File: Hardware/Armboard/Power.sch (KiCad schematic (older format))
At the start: 15 parts

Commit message: H-Bridge completed
Completed the H-Bridge Hierarchal Sheet
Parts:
- J?: symbol MRDT_Connectors:Test_Point -> Armboard-rescue:Test_Point-MRDT_Connectors
- U?: symbol MRDT_Devices:LM2576D2TR4 -> Armboard-rescue:LM2576D2TR4-MRDT_Devices
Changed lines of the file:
@@
 $EndComp
 $Comp
-L MRDT_Devices:LM2576D2TR4 U?
+L Armboard-rescue:LM2576D2TR4-MRDT_Devices U?
 U 1 1 5F74DE4A
 P 2100 3900
@@
 	3800 4250 3800 4200
 $Comp
-L MRDT_Connectors:Test_Point J?
+L Armboard-rescue:Test_Point-MRDT_Connectors J?
 U 1 1 5F75C39D
 P 4550 3950

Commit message: Added serial pins, limit switches, titles, and indicators
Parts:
- removed D?: D_Zener, symbol Device:D_Zener
- added Conn? (x6): AndersonPP, symbol Armboard-rescue:AndersonPP-MRDT_Connectors-Armboard-rescue-Armboard-rescue-Armb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
- added D?: D_Schottky, symbol Device:D_Schottky
- added D? (x2): LED, symbol Device:LED
- added R?: 500, symbol Device:R
- added R?: 330, symbol Device:R
- J?: symbol Armboard-rescue:Test_Point-MRDT_Connectors -> Armboard-rescue:Test_Point-MRDT_Connectors-Armboard-rescue
- U?: symbol Armboard-rescue:LM2576D2TR4-MRDT_Devices -> Armboard-rescue:LM2576D2TR4-MRDT_Devices-Armboard-rescue
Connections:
- net +12V: now also R?.2
- net +12VA: now also Conn?.3 (V+Act), Conn?.3 (V+Act), Conn?.3 (V+Act)
- net +3V3: now also R?.2
- net GND: now also Conn?.1 (GND), Conn?.1 (GND), Conn?.1 (GND), D?.1 (K), D?.1 (K), D?.1 (K)
- net at L?.2, U?.2 (OUTPUT): now also D?.2 (A)
- new net: D?.2 (A), R?.1 (x2)
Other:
- note added: "Output Andersons"
- note added: "Power"
- moved on the sheet: C7, C8, D?, J?, L?, R?, U?

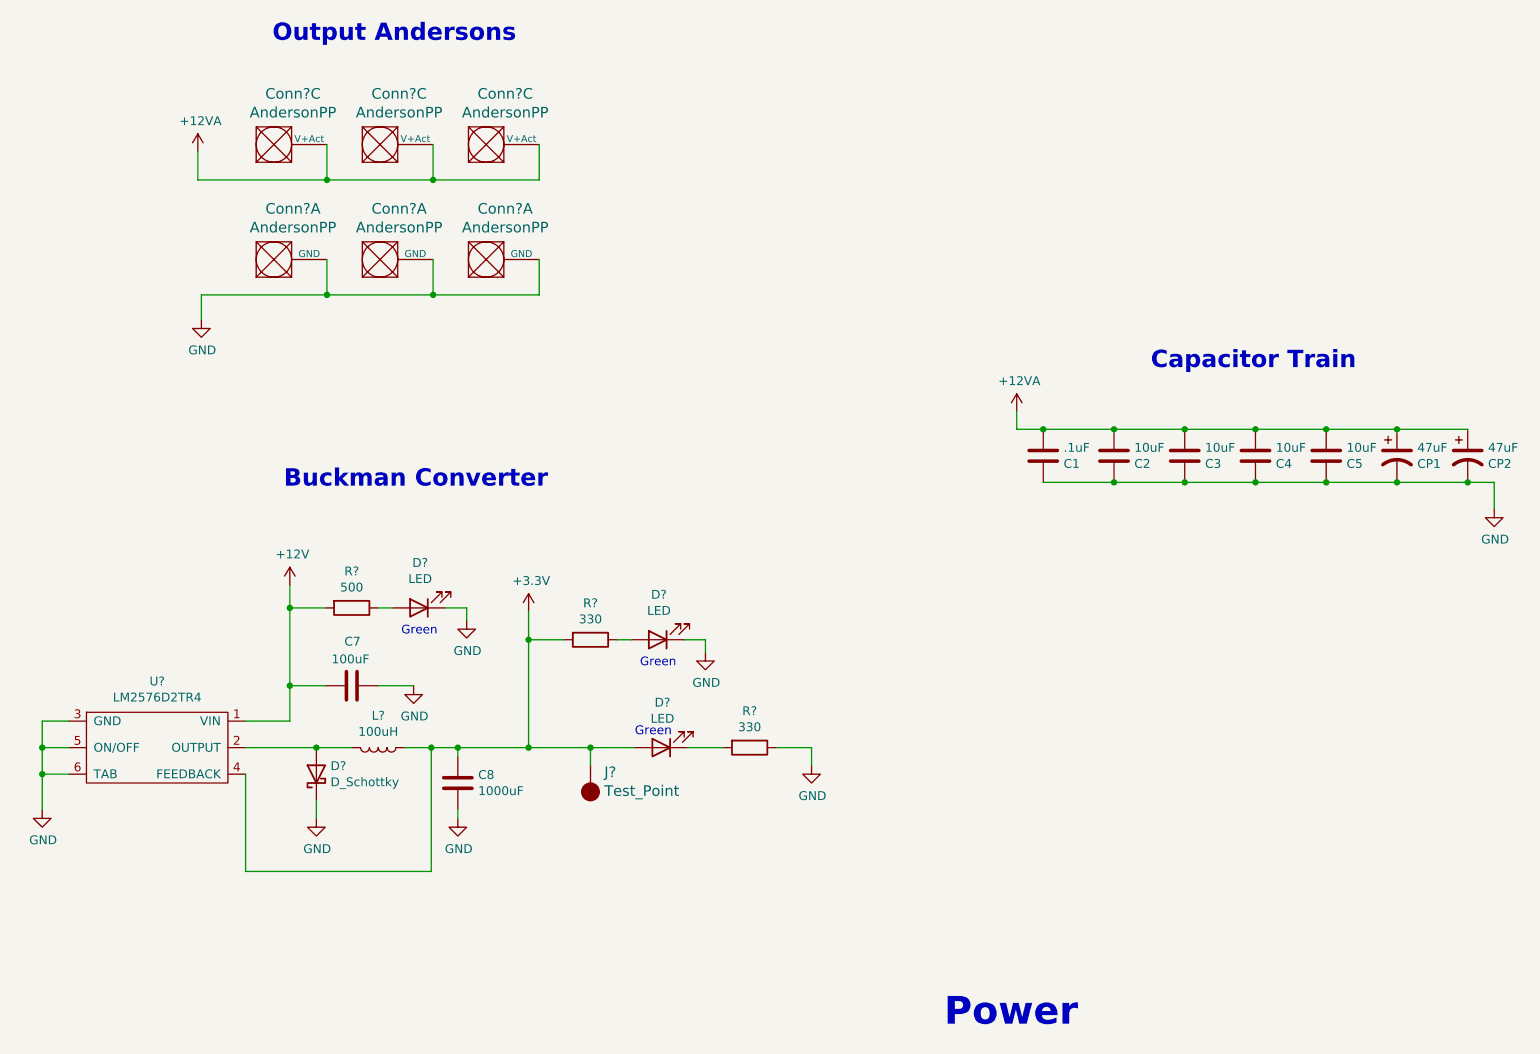
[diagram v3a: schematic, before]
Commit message: Moved I/O outside of Power block
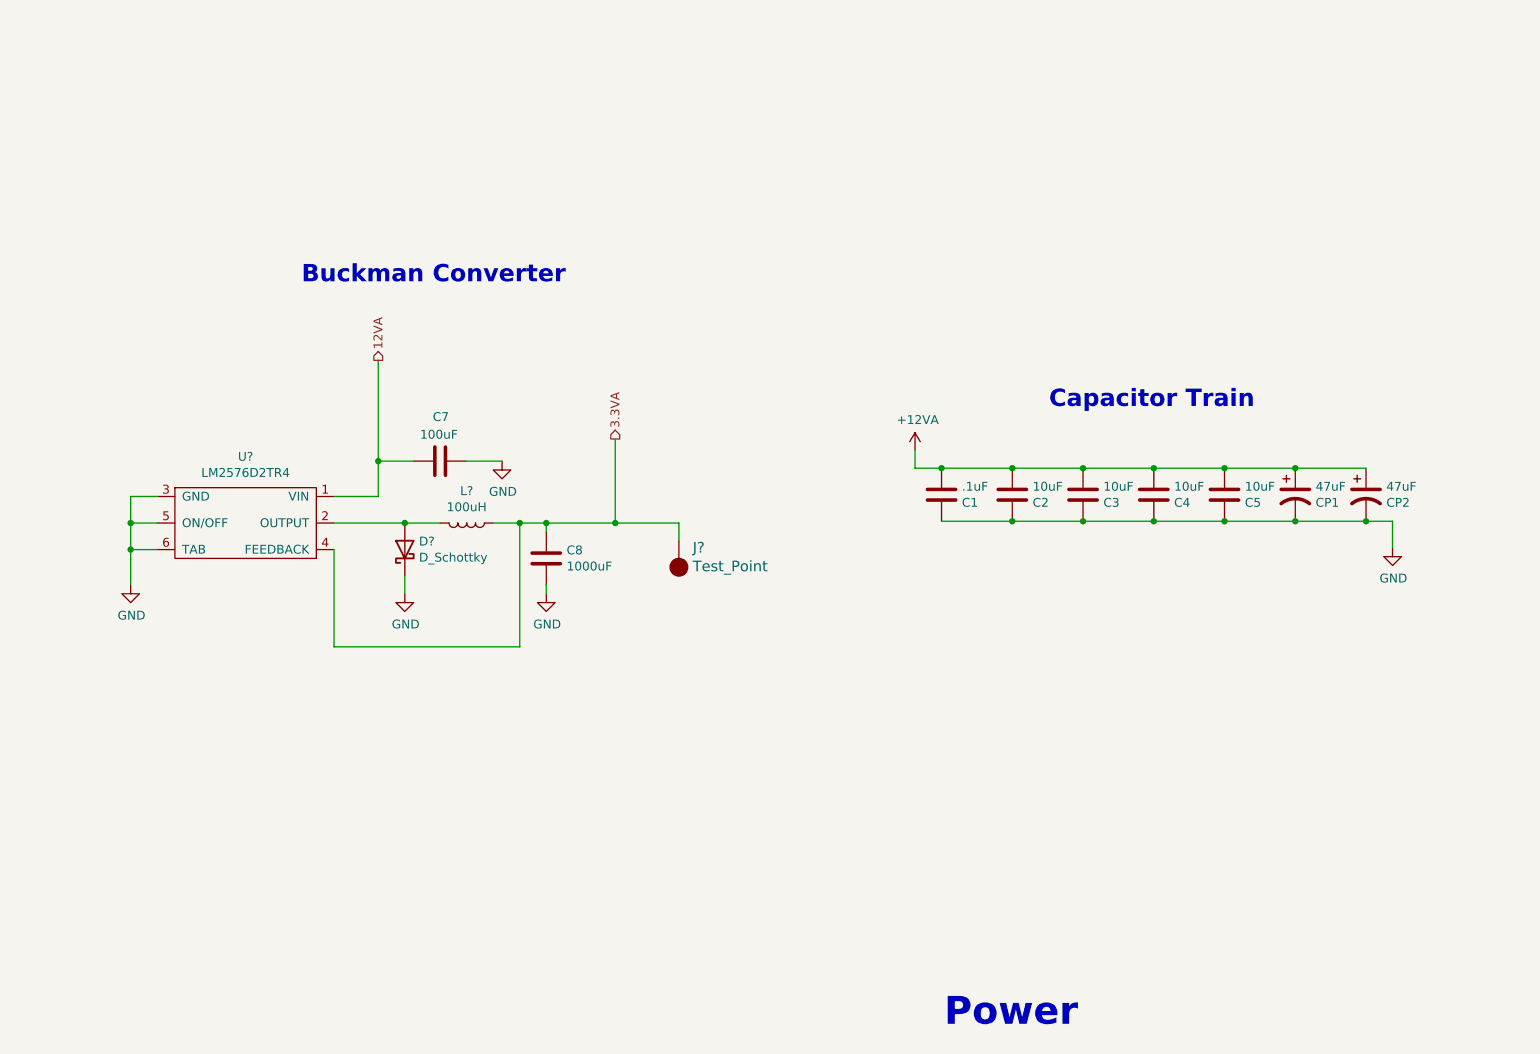
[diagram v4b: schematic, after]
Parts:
- removed Conn? (x6): AndersonPP, symbol Armboard-rescue:AndersonPP-MRDT_Connectors-Armboard-rescue-Armboard-rescue-Armb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
- removed D? (x3): LED, symbol Device:LED
- removed R? (x2): 330, symbol Device:R
- removed R?: 500, symbol Device:R
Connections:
- net +12V renamed 12VA
- net +3V3 renamed 3.3VA
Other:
- note removed: "Green"
- note removed: "Output Andersons"
- moved on the sheet: .1uF, 10uF, 47uF, C7, C8, D?, J?, L?, U?

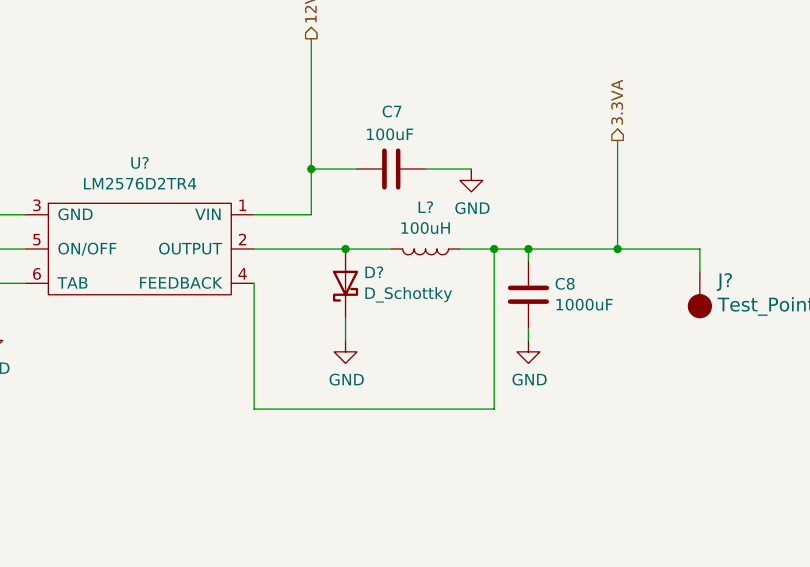
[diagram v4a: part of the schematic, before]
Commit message: Review 2 board changes
-Connected the busses on the power and H-Bridge
-Changed the resistor value to 1.2k
-Fixed some of the pin locations on the TIVA
-Added ferrites to the H-Bridge
-Connected the buses so that they all highlight correctly
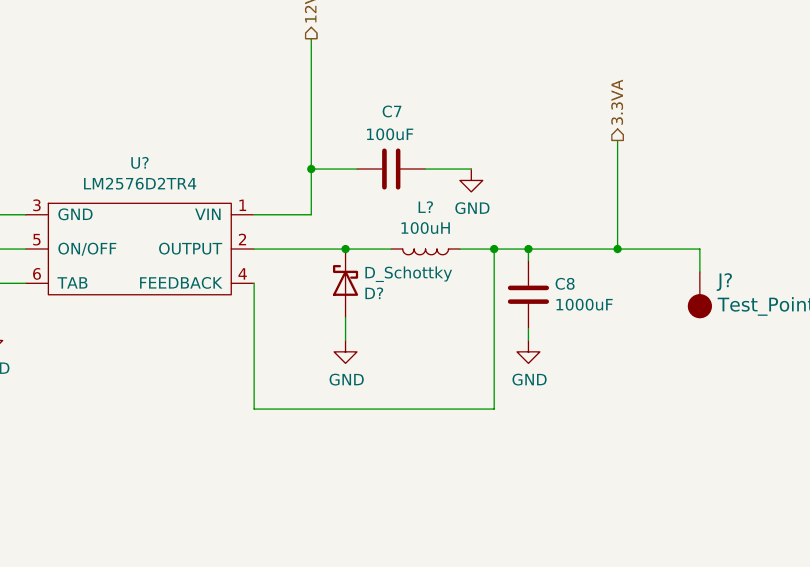
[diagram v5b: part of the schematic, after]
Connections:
- net GND: now also D?.2 (A); no longer D?.1 (K)
- net at L?.2, U?.2 (OUTPUT): now also D?.1 (K); no longer D?.2 (A)
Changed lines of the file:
@@
 F 3 "~" H 3570 4420 50  0001 C CNN
 	1    3570 4420
-	0    -1   -1   0
+	0    -1   1    0
 $EndComp
 Wire Wire Line

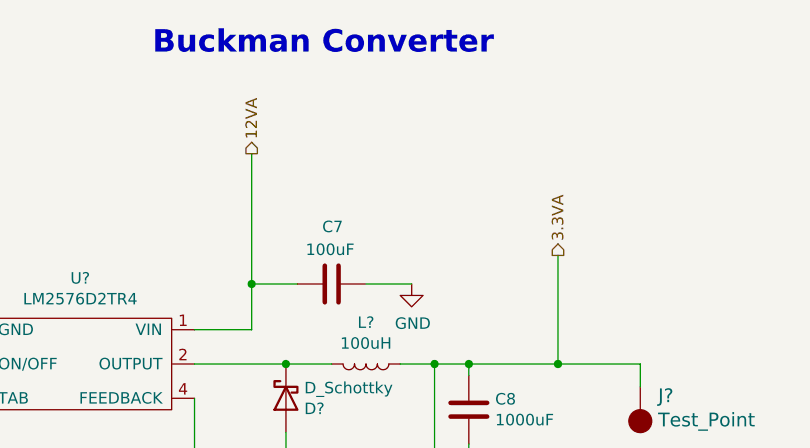
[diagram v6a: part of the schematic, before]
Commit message: Attempted to add 12 VL line
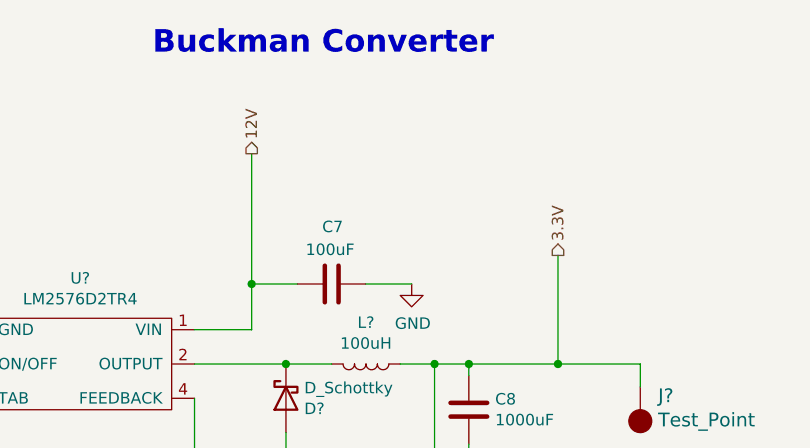
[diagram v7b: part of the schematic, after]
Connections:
- net 12VA renamed 12V
- net 3.3VA renamed 3.3V
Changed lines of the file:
@@
 Power
 Text HLabel 4760 3795 1    50   Output ~ 0
-3.3VA
+3.3V
 Text HLabel 3420 3350 1    50   Output ~ 0
-12VA
+12V
 Wire Wire Line
 	3420 3350 3420 3920

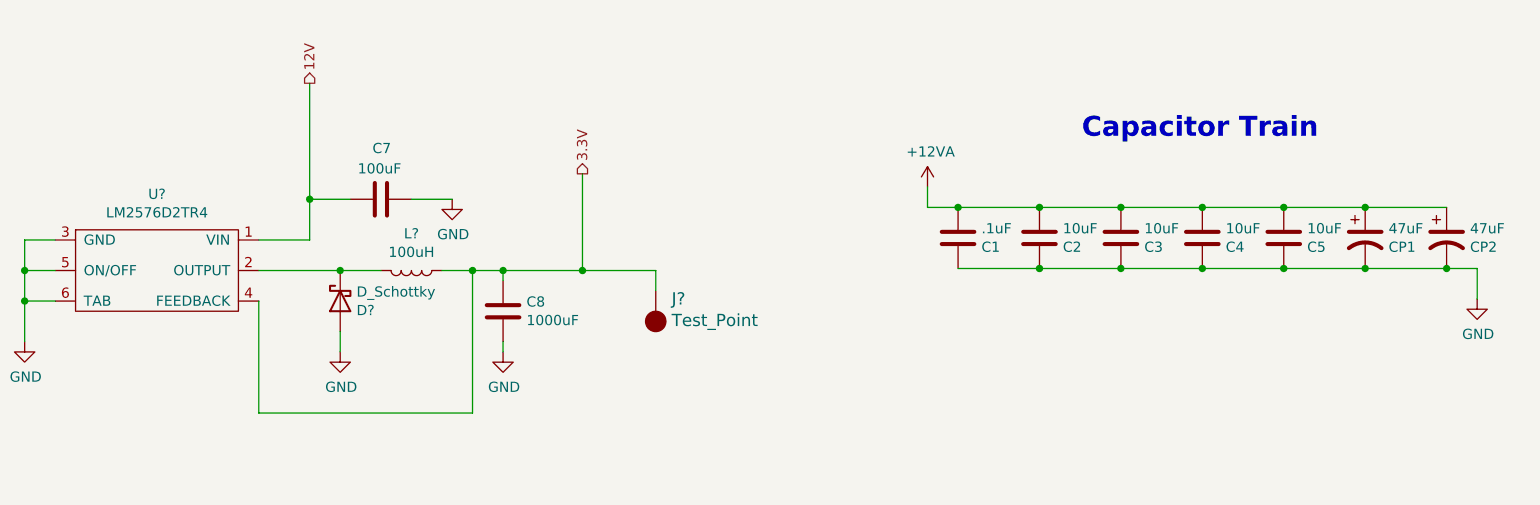
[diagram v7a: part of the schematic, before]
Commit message: Assigned R/L/C footprints
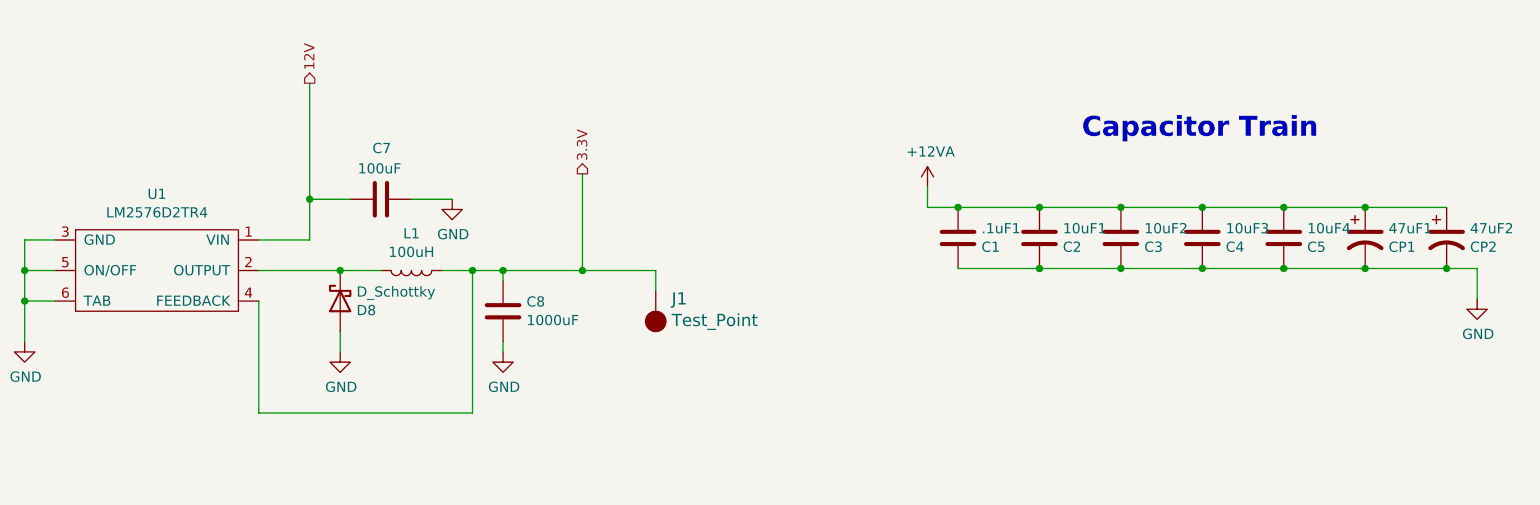
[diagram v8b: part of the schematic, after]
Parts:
- .1uF1: renamed from .1uF; footprint (none) -> Capacitor_SMD:C_0603_1608Metric_Pad1.05x0.95mm_HandSolder
- 10uF1, 10uF2, 10uF3, 10uF4: renamed from 10uF; footprint (none) -> Capacitor_SMD:C_0603_1608Metric_Pad1.05x0.95mm_HandSolder
- C7, C8: footprint (none) -> Capacitor_SMD:C_0603_1608Metric_Pad1.05x0.95mm_HandSolder
- L1: renamed from L?; footprint (none) -> Inductor_SMD:L_0603_1608Metric_Pad1.05x0.95mm_HandSolder
- gave numbers to parts that had none: 3
- renumbered 47uF to 47uF1, 47uF to 47uF2
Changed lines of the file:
@@
 $EndDescr
 $Comp
-L Device:C .1uF
+L Device:C .1uF1
 U 1 1 5F67AED3
 P 6605 4110
-F 0 ".1uF" H 6720 4156 50  0000 L CNN
+F 0 ".1uF1" H 6720 4156 50  0000 L CNN
 F 1 "C1" H 6720 4065 50  0000 L CNN
-F 2 "" H 6643 3960 50  0001 C CNN
+F 2 "Capacitor_SMD:C_0603_1608Metric_Pad1.05x0.95mm_HandSolder" H 6643 3960 50  0001 C CNN
 F 3 "~" H 6605 4110 50  0001 C CNN
 	1    6605 4110
@@
 $EndComp
 $Comp
-L Device:C 10uF
+L Device:C 10uF1
 U 1 1 5F67B379
 P 7005 4110
-F 0 "10uF" H 7120 4156 50  0000 L CNN
+F 0 "10uF1" H 7120 4156 50  0000 L CNN
 F 1 "C2" H 7120 4065 50  0000 L CNN
-F 2 "" H 7043 3960 50  0001 C CNN
+F 2 "Capacitor_SMD:C_0603_1608Metric_Pad1.05x0.95mm_HandSolder" H 7043 3960 50  0001 C CNN
 F 3 "~" H 7005 4110 50  0001 C CNN
 	1    7005 4110
@@
 $EndComp
 $Comp
-L Device:C 10uF
+L Device:C 10uF2
 U 1 1 5F67B840
 P 7405 4110
-F 0 "10uF" H 7520 4156 50  0000 L CNN
+F 0 "10uF2" H 7520 4156 50  0000 L CNN
 F 1 "C3" H 7520 4065 50  0000 L CNN
-F 2 "" H 7443 3960 50  0001 C CNN
+F 2 "Capacitor_SMD:C_0603_1608Metric_Pad1.05x0.95mm_HandSolder" H 7443 3960 50  0001 C CNN
 F 3 "~" H 7405 4110 50  0001 C CNN
 	1    7405 4110
@@
 $EndComp
 $Comp
-L Device:C 10uF
+L Device:C 10uF3
 U 1 1 5F67BE7A
 P 7805 4110
-F 0 "10uF" H 7920 4156 50  0000 L CNN
+F 0 "10uF3" H 7920 4156 50  0000 L CNN
 F 1 "C4" H 7920 4065 50  0000 L CNN
-F 2 "" H 7843 3960 50  0001 C CNN
+F 2 "Capacitor_SMD:C_0603_1608Metric_Pad1.05x0.95mm_HandSolder" H 7843 3960 50  0001 C CNN
 F 3 "~" H 7805 4110 50  0001 C CNN
 	1    7805 4110
@@
 $EndComp
 $Comp
-L Device:C 10uF
+L Device:C 10uF4
 U 1 1 5F67C26D
 P 8205 4110
-F 0 "10uF" H 8320 4156 50  0000 L CNN
+F 0 "10uF4" H 8320 4156 50  0000 L CNN
 F 1 "C5" H 8320 4065 50  0000 L CNN
-F 2 "" H 8243 3960 50  0001 C CNN
+F 2 "Capacitor_SMD:C_0603_1608Metric_Pad1.05x0.95mm_HandSolder" H 8243 3960 50  0001 C CNN
 F 3 "~" H 8205 4110 50  0001 C CNN
 	1    8205 4110
@@
 $EndComp
 $Comp
-L Device:CP1 47uF
+L Device:CP1 47uF1
 U 1 1 5F67C954
 P 8605 4110
-F 0 "47uF" H 8720 4156 50  0000 L CNN
+F 0 "47uF1" H 8720 4156 50  0000 L CNN
 F 1 "CP1" H 8720 4065 50  0000 L CNN
 F 2 "" H 8605 4110 50  0001 C CNN
@@
 $EndComp
 $Comp
-L Device:CP1 47uF
+L Device:CP1 47uF2
 U 1 1 5F67D4A0
 P 9005 4110
-F 0 "47uF" H 9120 4156 50  0000 L CNN
+F 0 "47uF2" H 9120 4156 50  0000 L CNN
 F 1 "CP2" H 9120 4065 50  0000 L CNN
 F 2 "" H 9005 4110 50  0001 C CNN
@@
 	9005 4260 9155 4260
 $Comp
-L power:GND #PWR?
+L power:GND #PWR013
 U 1 1 5F6806B4
 P 9155 4410
-F 0 "#PWR?" H 9155 4160 50  0001 C CNN
+F 0 "#PWR013" H 9155 4160 50  0001 C CNN
 F 1 "GND" H 9160 4237 50  0000 C CNN
 F 2 "" H 9155 4410 50  0001 C CNN
@@
 $EndComp
 $Comp
-L power:+12VA #PWR?
+L power:+12VA #PWR012
 U 1 1 5F680B53
 P 6455 3860
-F 0 "#PWR?" H 6455 3710 50  0001 C CNN
+F 0 "#PWR012" H 6455 3710 50  0001 C CNN
 F 1 "+12VA" H 6470 4033 50  0000 C CNN
 F 2 "" H 6455 3860 50  0001 C CNN
@@
 $EndComp
 $Comp
-L Armboard-rescue:LM2576D2TR4-MRDT_Devices-Armboard-rescue U?
+L Armboard-rescue:LM2576D2TR4-MRDT_Devices-Armboard-rescue U1
 U 1 1 5F74DE4A
 P 2670 4320
-F 0 "U?" H 2670 4745 50  0000 C CNN
+F 0 "U1" H 2670 4745 50  0000 C CNN
 F 1 "LM2576D2TR4" H 2670 4654 50  0000 C CNN
 F 2 "" H 2670 4770 50  0001 C CNN
@@
 $EndComp
 $Comp
-L power:GND #PWR?
+L power:GND #PWR08
 U 1 1 5F74E2A1
 P 2020 4620
-F 0 "#PWR?" H 2020 4370 50  0001 C CNN
+F 0 "#PWR08" H 2020 4370 50  0001 C CNN
 F 1 "GND" H 2025 4447 50  0000 C CNN
 F 2 "" H 2020 4620 50  0001 C CNN
@@
 F 0 "C8" H 4485 4516 50  0000 L CNN
 F 1 "1000uF" H 4485 4425 50  0000 L CNN
-F 2 "" H 4408 4320 50  0001 C CNN
+F 2 "Capacitor_SMD:C_0603_1608Metric_Pad1.05x0.95mm_HandSolder" H 4408 4320 50  0001 C CNN
 F 3 "~" H 4370 4470 50  0001 C CNN
 	1    4370 4470
@@
 F 0 "C7" V 4020 3870 50  0000 L CNN
 F 1 "100uF" V 3920 3820 50  0000 L CNN
-F 2 "" H 3808 3770 50  0001 C CNN
+F 2 "Capacitor_SMD:C_0603_1608Metric_Pad1.05x0.95mm_HandSolder" H 3808 3770 50  0001 C CNN
 F 3 "~" H 3770 3920 50  0001 C CNN
 	1    3770 3920
@@
 Connection ~ 3420 3920
 $Comp
-L power:GND #PWR?
+L power:GND #PWR010
 U 1 1 5F75423C
 P 4120 3920
-F 0 "#PWR?" H 4120 3670 50  0001 C CNN
+F 0 "#PWR010" H 4120 3670 50  0001 C CNN
 F 1 "GND" H 4125 3747 50  0000 C CNN
 F 2 "" H 4120 3920 50  0001 C CNN
@@
 	3920 3920 4120 3920
 $Comp
-L Device:L L?
+L Device:L L1
 U 1 1 5F755388
 P 3920 4270
-F 0 "L?" V 3739 4270 50  0000 C CNN
+F 0 "L1" V 3739 4270 50  0000 C CNN
 F 1 "100uH" V 3830 4270 50  0000 C CNN
-F 2 "" H 3920 4270 50  0001 C CNN
+F 2 "Inductor_SMD:L_0603_1608Metric_Pad1.05x0.95mm_HandSolder" H 3920 4270 50  0001 C CNN
 F 3 "~" H 3920 4270 50  0001 C CNN
 	1    3920 4270
@@
 $EndComp
 $Comp
-L power:GND #PWR?
+L power:GND #PWR09
 U 1 1 5F75782E
 P 3570 4670
-F 0 "#PWR?" H 3570 4420 50  0001 C CNN
+F 0 "#PWR09" H 3570 4420 50  0001 C CNN
 F 1 "GND" H 3575 4497 50  0000 C CNN
 F 2 "" H 3570 4670 50  0001 C CNN
@@
 	4220 4270 4370 4270
 $Comp
-L power:GND #PWR?
+L power:GND #PWR011
 U 1 1 5F75A24F
 P 4370 4670
-F 0 "#PWR?" H 4370 4420 50  0001 C CNN
+F 0 "#PWR011" H 4370 4420 50  0001 C CNN
 F 1 "GND" H 4375 4497 50  0000 C CNN
 F 2 "" H 4370 4670 50  0001 C CNN
@@
 	4370 4670 4370 4620
 $Comp
-L Armboard-rescue:Test_Point-MRDT_Connectors-Armboard-rescue J?
+L Armboard-rescue:Test_Point-MRDT_Connectors-Armboard-rescue J1
 U 1 1 5F75C39D
 P 5120 4370
-F 0 "J?" H 5042 4409 60  0000 R CNN
+F 0 "J1" H 5042 4409 60  0000 R CNN
 F 1 "Test_Point" H 5042 4515 60  0000 R CNN
 F 2 "" H 5120 4320 60  0001 C CNN
@@
 Capacitor Train
 $Comp
-L Device:D_Schottky D?
+L Device:D_Schottky D8
 U 1 1 5F83C9A2
 P 3570 4420
-F 0 "D?" V 3616 4340 50  0000 R CNN
+F 0 "D8" V 3616 4340 50  0000 R CNN
 F 1 "D_Schottky" V 3525 4340 50  0000 R CNN
 F 2 "" H 3570 4420 50  0001 C CNN
